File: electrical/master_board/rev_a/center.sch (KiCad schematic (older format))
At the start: 0 parts

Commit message: Updated some of the schematics and PCB's via hr2_models.py .
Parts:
- added CN50, CN54: HCSR04;F1X4, HR2:HCSR04_F1x4_MATE, symbol HR2:HCSR04;F1X4
- added CN51, CN52, CN53: HCSR04LP;F1X4, HR2:HCSR04_F1x4LP_MATE, symbol HR2:HCSR04LP;F1X4
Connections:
- no-connect marks 0 -> 20
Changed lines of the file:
@@
 Comment4 ""
 $EndDescr
+$Comp
+L HR2:HCSR04;F1X4 CN50
+U 1 1 5EE6C5CE
+P 2350 2550
+F 0 "CN50" H 2700 2700 50  0000 C CNN
+F 1 "HCSR04;F1X4" H 2700 2100 50  0000 C CNN
+F 2 "HR2:HCSR04_F1x4_MATE" H 2550 2600 60  0001 L CNN
+F 3 "https://cdn.sparkfun.com/datasheets/Sensors/Proximity/HCSR04.pdf" H 2550 2400 60  0001 L CNN
+F 4 "https://cdn.sparkfun.com/datasheets/Sensors/Proximity/HCSR04.pdf" H 2550 2500 60  0001 L CNN "manf#"
+F 5 "HC-SR04 Sonar (Normal Profile Receptacle)" H 2550 2300 60  0001 L CNN "Field5"
+	1    2350 2550
+	1    0    0    -1
+$EndComp
+$Comp
+L HR2:HCSR04;F1X4 CN54
+U 1 1 5EE6FA61
+P 5700 2550
+F 0 "CN54" H 6050 2700 50  0000 C CNN
+F 1 "HCSR04;F1X4" H 6050 2100 50  0000 C CNN
+F 2 "HR2:HCSR04_F1x4_MATE" H 5900 2600 60  0001 L CNN
+F 3 "https://cdn.sparkfun.com/datasheets/Sensors/Proximity/HCSR04.pdf" H 5900 2400 60  0001 L CNN
+F 4 "https://cdn.sparkfun.com/datasheets/Sensors/Proximity/HCSR04.pdf" H 5900 2500 60  0001 L CNN "manf#"
+F 5 "HC-SR04 Sonar (Normal Profile Receptacle)" H 5900 2300 60  0001 L CNN "Field5"
+	1    5700 2550
+	1    0    0    -1
+$EndComp
+NoConn ~ 3050 2550
+NoConn ~ 3050 2650
+NoConn ~ 3050 2750
+NoConn ~ 3050 2850
+NoConn ~ 3900 2550
+NoConn ~ 3900 2650
+NoConn ~ 3900 2750
+NoConn ~ 3900 2850
+NoConn ~ 4700 2550
+NoConn ~ 4700 2650
+NoConn ~ 4700 2750
+NoConn ~ 4700 2850
+NoConn ~ 5550 2550
+NoConn ~ 5550 2650
+NoConn ~ 5550 2750
+NoConn ~ 5550 2850
+NoConn ~ 6400 2550
+NoConn ~ 6400 2650
+NoConn ~ 6400 2750
+NoConn ~ 6400 2850
+$Comp
+L HR2:HCSR04LP;F1X4 CN51
+U 1 1 5EE6C7AA
+P 3200 2550
+F 0 "CN51" H 3550 2700 50  0000 C CNN
+F 1 "HCSR04LP;F1X4" H 3550 2100 50  0000 C CNN
+F 2 "HR2:HCSR04_F1x4LP_MATE" H 3400 2600 60  0001 L CNN
+F 3 "https://cdn.sparkfun.com/datasheets/Sensors/Proximity/HCSR04.pdf" H 3400 2400 60  0001 L CNN
+F 4 "https://cdn.sparkfun.com/datasheets/Sensors/Proximity/HCSR04.pdf" H 3400 2500 60  0001 L CNN "manf#"
+F 5 "HC-SR04 Sonar (Low Profile Receptacle)" H 3400 2300 60  0001 L CNN "Field5"
+	1    3200 2550
+	1    0    0    -1
+$EndComp
+$Comp
+L HR2:HCSR04LP;F1X4 CN52
+U 1 1 5EE6CD06
+P 4000 2550
+F 0 "CN52" H 4350 2700 50  0000 C CNN
+F 1 "HCSR04LP;F1X4" H 4350 2100 50  0000 C CNN
+F 2 "HR2:HCSR04_F1x4LP_MATE" H 4200 2600 60  0001 L CNN
+F 3 "https://cdn.sparkfun.com/datasheets/Sensors/Proximity/HCSR04.pdf" H 4200 2400 60  0001 L CNN
+F 4 "https://cdn.sparkfun.com/datasheets/Sensors/Proximity/HCSR04.pdf" H 4200 2500 60  0001 L CNN "manf#"
+F 5 "HC-SR04 Sonar (Low Profile Receptacle)" H 4200 2300 60  0001 L CNN "Field5"
+	1    4000 2550
+	1    0    0    -1
+$EndComp
+$Comp
+L HR2:HCSR04LP;F1X4 CN53
+U 1 1 5EE6D28F
+P 4850 2550
+F 0 "CN53" H 5200 2700 50  0000 C CNN
+F 1 "HCSR04LP;F1X4" H 5200 2100 50  0000 C CNN
+F 2 "HR2:HCSR04_F1x4LP_MATE" H 5050 2600 60  0001 L CNN
+F 3 "https://cdn.sparkfun.com/datasheets/Sensors/Proximity/HCSR04.pdf" H 5050 2400 60  0001 L CNN
+F 4 "https://cdn.sparkfun.com/datasheets/Sensors/Proximity/HCSR04.pdf" H 5050 2500 60  0001 L CNN "manf#"
+F 5 "HC-SR04 Sonar (Low Profile Receptacle)" H 5050 2300 60  0001 L CNN "Field5"
+	1    4850 2550
+	1    0    0    -1
+$EndComp
 $EndSCHEMATC

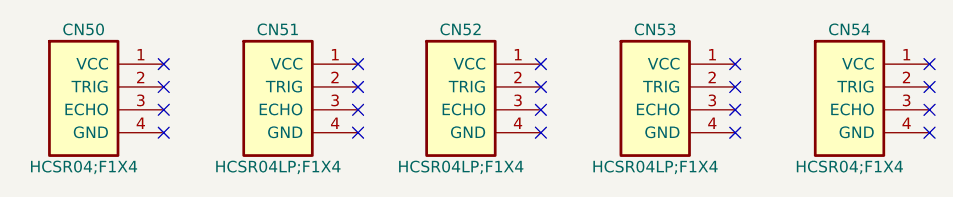
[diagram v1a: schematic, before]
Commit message: The PCBChunk'ification of Sonars is complete.
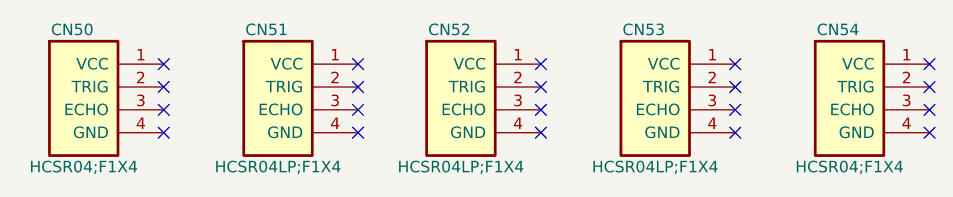
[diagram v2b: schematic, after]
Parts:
- CN50, CN54: footprint HR2:HCSR04_F1x4_MATE -> HR2:HCSR04_F1x4
- CN51, CN52, CN53: footprint HR2:HCSR04_F1x4LP_MATE -> HR2:HCSR04_F1x4LP
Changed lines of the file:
@@
 Comment4 ""
 $EndDescr
-$Comp
-L HR2:HCSR04;F1X4 CN50
-U 1 1 5EE6C5CE
-P 2350 2550
-F 0 "CN50" H 2700 2700 50  0000 C CNN
-F 1 "HCSR04;F1X4" H 2700 2100 50  0000 C CNN
-F 2 "HR2:HCSR04_F1x4_MATE" H 2550 2600 60  0001 L CNN
-F 3 "https://cdn.sparkfun.com/datasheets/Sensors/Proximity/HCSR04.pdf" H 2550 2400 60  0001 L CNN
-F 4 "https://cdn.sparkfun.com/datasheets/Sensors/Proximity/HCSR04.pdf" H 2550 2500 60  0001 L CNN "manf#"
-F 5 "HC-SR04 Sonar (Normal Profile Receptacle)" H 2550 2300 60  0001 L CNN "Field5"
-	1    2350 2550
-	1    0    0    -1
-$EndComp
-$Comp
-L HR2:HCSR04;F1X4 CN54
-U 1 1 5EE6FA61
-P 5700 2550
-F 0 "CN54" H 6050 2700 50  0000 C CNN
-F 1 "HCSR04;F1X4" H 6050 2100 50  0000 C CNN
-F 2 "HR2:HCSR04_F1x4_MATE" H 5900 2600 60  0001 L CNN
-F 3 "https://cdn.sparkfun.com/datasheets/Sensors/Proximity/HCSR04.pdf" H 5900 2400 60  0001 L CNN
-F 4 "https://cdn.sparkfun.com/datasheets/Sensors/Proximity/HCSR04.pdf" H 5900 2500 60  0001 L CNN "manf#"
-F 5 "HC-SR04 Sonar (Normal Profile Receptacle)" H 5900 2300 60  0001 L CNN "Field5"
-	1    5700 2550
-	1    0    0    -1
-$EndComp
 NoConn ~ 3050 2550
 NoConn ~ 3050 2650
@@
 $Comp
 L HR2:HCSR04LP;F1X4 CN51
-U 1 1 5EE6C7AA
+U 1 1 5F0BA517
 P 3200 2550
-F 0 "CN51" H 3550 2700 50  0000 C CNN
+F 0 "CN51" H 3500 2700 50  0000 C CNN
 F 1 "HCSR04LP;F1X4" H 3550 2100 50  0000 C CNN
-F 2 "HR2:HCSR04_F1x4LP_MATE" H 3400 2600 60  0001 L CNN
+F 2 "HR2:HCSR04_F1x4LP" H 3400 2600 60  0001 L CNN
 F 3 "https://cdn.sparkfun.com/datasheets/Sensors/Proximity/HCSR04.pdf" H 3400 2400 60  0001 L CNN
 F 4 "https://cdn.sparkfun.com/datasheets/Sensors/Proximity/HCSR04.pdf" H 3400 2500 60  0001 L CNN "manf#"
@@
 $Comp
 L HR2:HCSR04LP;F1X4 CN52
-U 1 1 5EE6CD06
+U 1 1 5F0BB7A6
 P 4000 2550
-F 0 "CN52" H 4350 2700 50  0000 C CNN
+F 0 "CN52" H 4300 2700 50  0000 C CNN
 F 1 "HCSR04LP;F1X4" H 4350 2100 50  0000 C CNN
-F 2 "HR2:HCSR04_F1x4LP_MATE" H 4200 2600 60  0001 L CNN
+F 2 "HR2:HCSR04_F1x4LP" H 4200 2600 60  0001 L CNN
 F 3 "https://cdn.sparkfun.com/datasheets/Sensors/Proximity/HCSR04.pdf" H 4200 2400 60  0001 L CNN
 F 4 "https://cdn.sparkfun.com/datasheets/Sensors/Proximity/HCSR04.pdf" H 4200 2500 60  0001 L CNN "manf#"
@@
 $Comp
 L HR2:HCSR04LP;F1X4 CN53
-U 1 1 5EE6D28F
+U 1 1 5F0BBC9F
 P 4850 2550
-F 0 "CN53" H 5200 2700 50  0000 C CNN
+F 0 "CN53" H 5150 2700 50  0000 C CNN
 F 1 "HCSR04LP;F1X4" H 5200 2100 50  0000 C CNN
-F 2 "HR2:HCSR04_F1x4LP_MATE" H 5050 2600 60  0001 L CNN
+F 2 "HR2:HCSR04_F1x4LP" H 5050 2600 60  0001 L CNN
 F 3 "https://cdn.sparkfun.com/datasheets/Sensors/Proximity/HCSR04.pdf" H 5050 2400 60  0001 L CNN
 F 4 "https://cdn.sparkfun.com/datasheets/Sensors/Proximity/HCSR04.pdf" H 5050 2500 60  0001 L CNN "manf#"
@@
 	1    0    0    -1
 $EndComp
+$Comp
+L HR2:HCSR04;F1X4 CN50
+U 1 1 5F0B87B8
+P 2350 2550
+F 0 "CN50" H 2650 2700 50  0000 C CNN
+F 1 "HCSR04;F1X4" H 2700 2100 50  0000 C CNN
+F 2 "HR2:HCSR04_F1x4" H 2550 2600 60  0001 L CNN
+F 3 "https://cdn.sparkfun.com/datasheets/Sensors/Proximity/HCSR04.pdf" H 2550 2400 60  0001 L CNN
+F 4 "https://cdn.sparkfun.com/datasheets/Sensors/Proximity/HCSR04.pdf" H 2550 2500 60  0001 L CNN "manf#"
+F 5 "HC-SR04 Sonar (Normal Profile Receptacle)" H 2550 2300 60  0001 L CNN "Field5"
+	1    2350 2550
+	1    0    0    -1
+$EndComp
+$Comp
+L HR2:HCSR04;F1X4 CN54
+U 1 1 5F0B915D
+P 5700 2550
+F 0 "CN54" H 6000 2700 50  0000 C CNN
+F 1 "HCSR04;F1X4" H 6050 2100 50  0000 C CNN
+F 2 "HR2:HCSR04_F1x4" H 5900 2600 60  0001 L CNN
+F 3 "https://cdn.sparkfun.com/datasheets/Sensors/Proximity/HCSR04.pdf" H 5900 2400 60  0001 L CNN
+F 4 "https://cdn.sparkfun.com/datasheets/Sensors/Proximity/HCSR04.pdf" H 5900 2500 60  0001 L CNN "manf#"
+F 5 "HC-SR04 Sonar (Normal Profile Receptacle)" H 5900 2300 60  0001 L CNN "Field5"
+	1    5700 2550
+	1    0    0    -1
+$EndComp

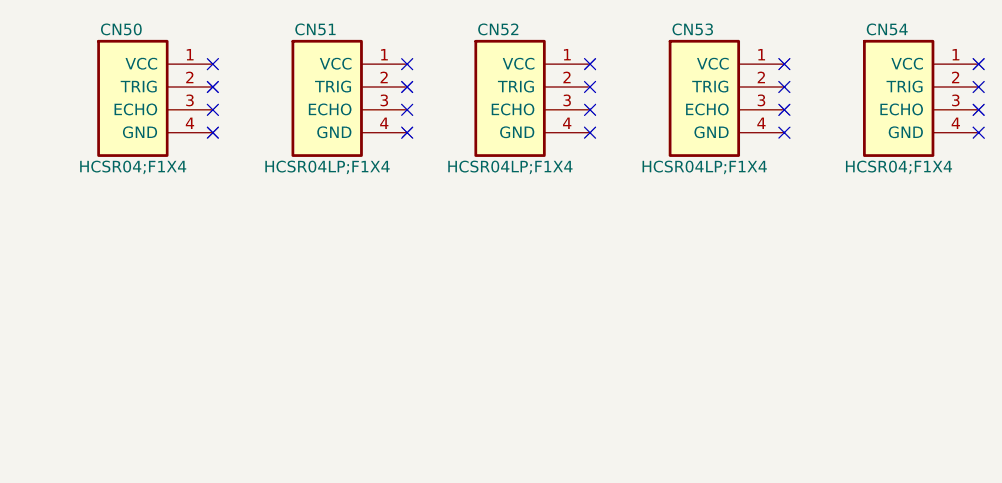
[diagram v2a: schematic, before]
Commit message: Got Encoder PCB's installed on the center PCB.
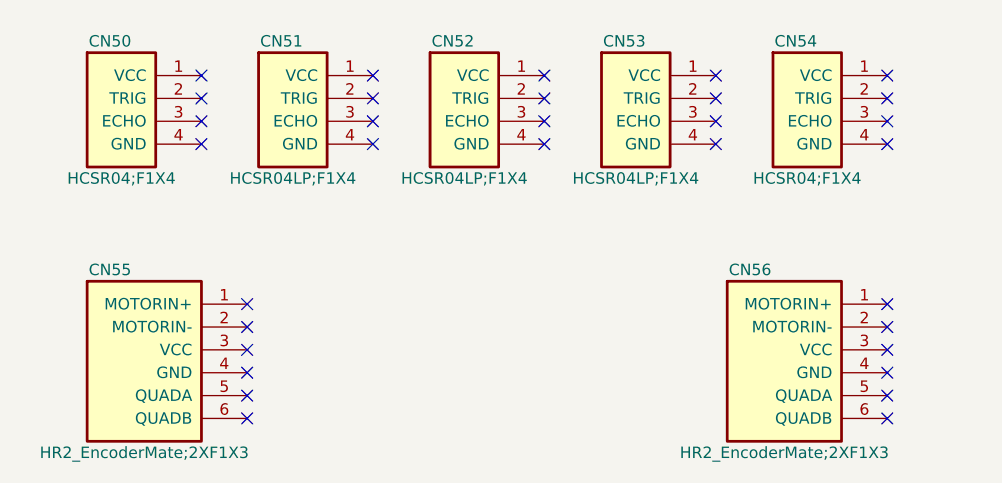
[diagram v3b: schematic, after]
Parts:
- added CN55, CN56: HR2_EncoderMate;2XF1X3, HR2:ENCODER_MATE, symbol HR2:HR2_EncoderMate;2XF1X3
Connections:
- no-connect marks 20 -> 32
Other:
- moved on the sheet: CN50, CN51, CN52, CN53, CN54
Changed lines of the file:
@@
 Comment4 ""
 $EndDescr
-NoConn ~ 3050 2550
-NoConn ~ 3050 2650
-NoConn ~ 3050 2750
-NoConn ~ 3050 2850
-NoConn ~ 3900 2550
-NoConn ~ 3900 2650
-NoConn ~ 3900 2750
-NoConn ~ 3900 2850
-NoConn ~ 4700 2550
-NoConn ~ 4700 2650
-NoConn ~ 4700 2750
-NoConn ~ 4700 2850
-NoConn ~ 5550 2550
-NoConn ~ 5550 2650
-NoConn ~ 5550 2750
-NoConn ~ 5550 2850
-NoConn ~ 6400 2550
-NoConn ~ 6400 2650
-NoConn ~ 6400 2750
-NoConn ~ 6400 2850
+NoConn ~ 3000 2600
+NoConn ~ 3000 2700
+NoConn ~ 3000 2800
+NoConn ~ 3000 2900
+NoConn ~ 3750 2600
+NoConn ~ 3750 2700
+NoConn ~ 3750 2800
+NoConn ~ 3750 2900
+NoConn ~ 4500 2600
+NoConn ~ 4500 2700
+NoConn ~ 4500 2800
+NoConn ~ 4500 2900
+NoConn ~ 5250 2600
+NoConn ~ 5250 2700
+NoConn ~ 5250 2800
+NoConn ~ 5250 2900
+NoConn ~ 6000 2600
+NoConn ~ 6000 2700
+NoConn ~ 6000 2800
+NoConn ~ 6000 2900
 $Comp
 L HR2:HCSR04LP;F1X4 CN51
 U 1 1 5F0BA517
-P 3200 2550
-F 0 "CN51" H 3500 2700 50  0000 C CNN
-F 1 "HCSR04LP;F1X4" H 3550 2100 50  0000 C CNN
-F 2 "HR2:HCSR04_F1x4LP" H 3400 2600 60  0001 L CNN
-F 3 "https://cdn.sparkfun.com/datasheets/Sensors/Proximity/HCSR04.pdf" H 3400 2400 60  0001 L CNN
-F 4 "https://cdn.sparkfun.com/datasheets/Sensors/Proximity/HCSR04.pdf" H 3400 2500 60  0001 L CNN "manf#"
-F 5 "HC-SR04 Sonar (Low Profile Receptacle)" H 3400 2300 60  0001 L CNN "Field5"
-	1    3200 2550
+P 3050 2600
+F 0 "CN51" H 3350 2750 50  0000 C CNN
+F 1 "HCSR04LP;F1X4" H 3400 2150 50  0000 C CNN
+F 2 "HR2:HCSR04_F1x4LP" H 3250 2650 60  0001 L CNN
+F 3 "https://cdn.sparkfun.com/datasheets/Sensors/Proximity/HCSR04.pdf" H 3250 2450 60  0001 L CNN
+F 4 "https://cdn.sparkfun.com/datasheets/Sensors/Proximity/HCSR04.pdf" H 3250 2550 60  0001 L CNN "manf#"
+F 5 "HC-SR04 Sonar (Low Profile Receptacle)" H 3250 2350 60  0001 L CNN "Field5"
+	1    3050 2600
 	1    0    0    -1
 $EndComp
@@
 L HR2:HCSR04LP;F1X4 CN52
 U 1 1 5F0BB7A6
-P 4000 2550
-F 0 "CN52" H 4300 2700 50  0000 C CNN
-F 1 "HCSR04LP;F1X4" H 4350 2100 50  0000 C CNN
-F 2 "HR2:HCSR04_F1x4LP" H 4200 2600 60  0001 L CNN
-F 3 "https://cdn.sparkfun.com/datasheets/Sensors/Proximity/HCSR04.pdf" H 4200 2400 60  0001 L CNN
-F 4 "https://cdn.sparkfun.com/datasheets/Sensors/Proximity/HCSR04.pdf" H 4200 2500 60  0001 L CNN "manf#"
-F 5 "HC-SR04 Sonar (Low Profile Receptacle)" H 4200 2300 60  0001 L CNN "Field5"
-	1    4000 2550
+P 3800 2600
+F 0 "CN52" H 4100 2750 50  0000 C CNN
+F 1 "HCSR04LP;F1X4" H 4150 2150 50  0000 C CNN
+F 2 "HR2:HCSR04_F1x4LP" H 4000 2650 60  0001 L CNN
+F 3 "https://cdn.sparkfun.com/datasheets/Sensors/Proximity/HCSR04.pdf" H 4000 2450 60  0001 L CNN
+F 4 "https://cdn.sparkfun.com/datasheets/Sensors/Proximity/HCSR04.pdf" H 4000 2550 60  0001 L CNN "manf#"
+F 5 "HC-SR04 Sonar (Low Profile Receptacle)" H 4000 2350 60  0001 L CNN "Field5"
+	1    3800 2600
 	1    0    0    -1
 $EndComp
@@
 L HR2:HCSR04LP;F1X4 CN53
 U 1 1 5F0BBC9F
-P 4850 2550
-F 0 "CN53" H 5150 2700 50  0000 C CNN
-F 1 "HCSR04LP;F1X4" H 5200 2100 50  0000 C CNN
-F 2 "HR2:HCSR04_F1x4LP" H 5050 2600 60  0001 L CNN
-F 3 "https://cdn.sparkfun.com/datasheets/Sensors/Proximity/HCSR04.pdf" H 5050 2400 60  0001 L CNN
-F 4 "https://cdn.sparkfun.com/datasheets/Sensors/Proximity/HCSR04.pdf" H 5050 2500 60  0001 L CNN "manf#"
-F 5 "HC-SR04 Sonar (Low Profile Receptacle)" H 5050 2300 60  0001 L CNN "Field5"
-	1    4850 2550
+P 4550 2600
+F 0 "CN53" H 4850 2750 50  0000 C CNN
+F 1 "HCSR04LP;F1X4" H 4900 2150 50  0000 C CNN
+F 2 "HR2:HCSR04_F1x4LP" H 4750 2650 60  0001 L CNN
+F 3 "https://cdn.sparkfun.com/datasheets/Sensors/Proximity/HCSR04.pdf" H 4750 2450 60  0001 L CNN
+F 4 "https://cdn.sparkfun.com/datasheets/Sensors/Proximity/HCSR04.pdf" H 4750 2550 60  0001 L CNN "manf#"
+F 5 "HC-SR04 Sonar (Low Profile Receptacle)" H 4750 2350 60  0001 L CNN "Field5"
+	1    4550 2600
 	1    0    0    -1
 $EndComp
@@
 L HR2:HCSR04;F1X4 CN50
 U 1 1 5F0B87B8
-P 2350 2550
-F 0 "CN50" H 2650 2700 50  0000 C CNN
-F 1 "HCSR04;F1X4" H 2700 2100 50  0000 C CNN
-F 2 "HR2:HCSR04_F1x4" H 2550 2600 60  0001 L CNN
-F 3 "https://cdn.sparkfun.com/datasheets/Sensors/Proximity/HCSR04.pdf" H 2550 2400 60  0001 L CNN
-F 4 "https://cdn.sparkfun.com/datasheets/Sensors/Proximity/HCSR04.pdf" H 2550 2500 60  0001 L CNN "manf#"
-F 5 "HC-SR04 Sonar (Normal Profile Receptacle)" H 2550 2300 60  0001 L CNN "Field5"
-	1    2350 2550
+P 2300 2600
+F 0 "CN50" H 2600 2750 50  0000 C CNN
+F 1 "HCSR04;F1X4" H 2650 2150 50  0000 C CNN
+F 2 "HR2:HCSR04_F1x4" H 2500 2650 60  0001 L CNN
+F 3 "https://cdn.sparkfun.com/datasheets/Sensors/Proximity/HCSR04.pdf" H 2500 2450 60  0001 L CNN
+F 4 "https://cdn.sparkfun.com/datasheets/Sensors/Proximity/HCSR04.pdf" H 2500 2550 60  0001 L CNN "manf#"
+F 5 "HC-SR04 Sonar (Normal Profile Receptacle)" H 2500 2350 60  0001 L CNN "Field5"
+	1    2300 2600
 	1    0    0    -1
 $EndComp
@@
 L HR2:HCSR04;F1X4 CN54
 U 1 1 5F0B915D
-P 5700 2550
-F 0 "CN54" H 6000 2700 50  0000 C CNN
-F 1 "HCSR04;F1X4" H 6050 2100 50  0000 C CNN
-F 2 "HR2:HCSR04_F1x4" H 5900 2600 60  0001 L CNN
-F 3 "https://cdn.sparkfun.com/datasheets/Sensors/Proximity/HCSR04.pdf" H 5900 2400 60  0001 L CNN
-F 4 "https://cdn.sparkfun.com/datasheets/Sensors/Proximity/HCSR04.pdf" H 5900 2500 60  0001 L CNN "manf#"
-F 5 "HC-SR04 Sonar (Normal Profile Receptacle)" H 5900 2300 60  0001 L CNN "Field5"
-	1    5700 2550
+P 5300 2600
+F 0 "CN54" H 5600 2750 50  0000 C CNN
+F 1 "HCSR04;F1X4" H 5650 2150 50  0000 C CNN
+F 2 "HR2:HCSR04_F1x4" H 5500 2650 60  0001 L CNN
+F 3 "https://cdn.sparkfun.com/datasheets/Sensors/Proximity/HCSR04.pdf" H 5500 2450 60  0001 L CNN
+F 4 "https://cdn.sparkfun.com/datasheets/Sensors/Proximity/HCSR04.pdf" H 5500 2550 60  0001 L CNN "manf#"
+F 5 "HC-SR04 Sonar (Normal Profile Receptacle)" H 5500 2350 60  0001 L CNN "Field5"
+	1    5300 2600
 	1    0    0    -1
 $EndComp
+NoConn ~ 3200 3600
+NoConn ~ 3200 3700
+NoConn ~ 3200 3800
+NoConn ~ 3200 3900
+NoConn ~ 3200 4000
+NoConn ~ 3200 4100
+$Comp
+L HR2:HR2_EncoderMate;2XF1X3 CN55
+U 1 1 5F0BB3ED
+P 2300 3600
+F 0 "CN55" H 2600 3750 50  0000 C CNN
+F 1 "HR2_EncoderMate;2XF1X3" H 2750 2950 50  0000 C CNN
+F 2 "HR2:ENCODER_MATE" H 2500 3650 60  0001 L CNN
+F 3 "HR2 Encoder Mating Connector" H 2500 3450 60  0001 L CNN
+F 4 "HR2 Encoder Mating Connector" H 2500 3350 60  0001 L CNN "Field5"
+	1    2300 3600
+	1    0    0    -1
+$EndComp
+NoConn ~ 6000 4100
+NoConn ~ 6000 4000
+NoConn ~ 6000 3900
+NoConn ~ 6000 3800
+NoConn ~ 6000 3700
+NoConn ~ 6000 3600
+$Comp
+L HR2:HR2_EncoderMate;2XF1X3 CN56
+U 1 1 5F0BC2D6
+P 5100 3600
+F 0 "CN56" H 5400 3750 50  0000 C CNN
+F 1 "HR2_EncoderMate;2XF1X3" H 5550 2950 50  0000 C CNN
+F 2 "HR2:ENCODER_MATE" H 5300 3650 60  0001 L CNN
+F 3 "HR2 Encoder Mating Connector" H 5300 3450 60  0001 L CNN
+F 4 "HR2 Encoder Mating Connector" H 5300 3350 60  0001 L CNN "Field5"
+	1    5100 3600
+	1    0    0    -1
+$EndComp

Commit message: Added Raspbery Pi F2x20 Connector to schematic library.
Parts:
- added CN57: RASPI;F2X20;HR2_RASPI_F2X20, symbol HR2:RASPI;F2X20;HR2_RASPI_F2X20
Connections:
- no-connect marks 32 -> 72
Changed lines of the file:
@@
-	1    0    0    -1
-$EndComp
-$Comp
-L HR2:HCSR04;F1X4 CN50
-U 1 1 5F0B87B8
-P 2300 2600
-F 0 "CN50" H 2600 2750 50  0000 C CNN
-F 1 "HCSR04;F1X4" H 2650 2150 50  0000 C CNN
-F 2 "HR2:HCSR04_F1x4" H 2500 2650 60  0001 L CNN
-F 3 "https://cdn.sparkfun.com/datasheets/Sensors/Proximity/HCSR04.pdf" H 2500 2450 60  0001 L CNN
-F 4 "https://cdn.sparkfun.com/datasheets/Sensors/Proximity/HCSR04.pdf" H 2500 2550 60  0001 L CNN "manf#"
-F 5 "HC-SR04 Sonar (Normal Profile Receptacle)" H 2500 2350 60  0001 L CNN "Field5"
-	1    2300 2600
-	1    0    0    -1
-$EndComp
-$Comp
-L HR2:HCSR04;F1X4 CN54
-U 1 1 5F0B915D
-P 5300 2600
-F 0 "CN54" H 5600 2750 50  0000 C CNN
-F 1 "HCSR04;F1X4" H 5650 2150 50  0000 C CNN
-F 2 "HR2:HCSR04_F1x4" H 5500 2650 60  0001 L CNN
-F 3 "https://cdn.sparkfun.com/datasheets/Sensors/Proximity/HCSR04.pdf" H 5500 2450 60  0001 L CNN
-F 4 "https://cdn.sparkfun.com/datasheets/Sensors/Proximity/HCSR04.pdf" H 5500 2550 60  0001 L CNN "manf#"
-F 5 "HC-SR04 Sonar (Normal Profile Receptacle)" H 5500 2350 60  0001 L CNN "Field5"
-	1    5300 2600
 	1    0    0    -1
 $EndComp
@@
 	1    0    0    -1
 $EndComp
+$Comp
+L HR2:HCSR04;F1X4 CN50
+U 1 1 5F0D2697
+P 2300 2600
+F 0 "CN50" H 2650 2750 50  0000 C CNN
+F 1 "HCSR04;F1X4" H 2650 2150 50  0000 C CNN
+F 2 "HR2:HCSR04_F1x4" H 2500 2650 60  0001 L CNN
+F 3 "HC-SR04" H 2500 2450 60  0001 L CNN
+F 4 "https://cdn.sparkfun.com/datasheets/Sensors/Proximity/HCSR04.pdf" H 2500 2550 60  0001 L CNN "manf#"
+F 5 "HC-SR04 Sonar (Normal Profile Receptacle)" H 2500 2350 60  0001 L CNN "Field5"
+	1    2300 2600
+	1    0    0    -1
+$EndComp
+$Comp
+L HR2:HCSR04;F1X4 CN54
+U 1 1 5F0D2FF0
+P 5300 2600
+F 0 "CN54" H 5650 2750 50  0000 C CNN
+F 1 "HCSR04;F1X4" H 5650 2150 50  0000 C CNN
+F 2 "HR2:HCSR04_F1x4" H 5500 2650 60  0001 L CNN
+F 3 "HC-SR04" H 5500 2450 60  0001 L CNN
+F 4 "https://cdn.sparkfun.com/datasheets/Sensors/Proximity/HCSR04.pdf" H 5500 2550 60  0001 L CNN "manf#"
+F 5 "HC-SR04 Sonar (Normal Profile Receptacle)" H 5500 2350 60  0001 L CNN "Field5"
+	1    5300 2600
+	1    0    0    -1
+$EndComp
+$Comp
+L HR2:RASPI;F2X20;HR2_RASPI_F2X20 CN57
+U 1 1 5F0D2725
+P 7600 1000
+F 0 "CN57" H 8050 1150 60  0000 C CNN
+F 1 "RASPI;F2X20;HR2_RASPI_F2X20" H 8050 -3050 60  0000 C CNN
+F 2 "" H 7800 1050 60  0001 L CNN
+F 3 "HR2 Raspberry Pi F2x20 Connector" H 7800 850 60  0001 L CNN
+	1    7600 1000
+	1    0    0    -1
+$EndComp
+NoConn ~ 8500 1000
+NoConn ~ 8500 1100
+NoConn ~ 8500 1200
+NoConn ~ 8500 1300
+NoConn ~ 8500 1400
+NoConn ~ 8500 1500
+NoConn ~ 8500 1600
+NoConn ~ 8500 1700
+NoConn ~ 8500 1800
+NoConn ~ 8500 1900
+NoConn ~ 8500 2000
+NoConn ~ 8500 2100
+NoConn ~ 8500 2200
+NoConn ~ 8500 2300
+NoConn ~ 8500 2400
+NoConn ~ 8500 2500
+NoConn ~ 8500 2600
+NoConn ~ 8500 2700
+NoConn ~ 8500 2800
+NoConn ~ 8500 2900
+NoConn ~ 8500 3000
+NoConn ~ 8500 3100
+NoConn ~ 8500 3200
+NoConn ~ 8500 3300
+NoConn ~ 8500 3400
+NoConn ~ 8500 3500
+NoConn ~ 8500 3600
+NoConn ~ 8500 3700
+NoConn ~ 8500 3800
+NoConn ~ 8500 3900
+NoConn ~ 8500 4000
+NoConn ~ 8500 4100
+NoConn ~ 8500 4900
+NoConn ~ 8500 4800
+NoConn ~ 8500 4700
+NoConn ~ 8500 4600
+NoConn ~ 8500 4500
+NoConn ~ 8500 4400
+NoConn ~ 8500 4300
+NoConn ~ 8500 4200
 $EndSCHEMATC

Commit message: Did initial placement of RasPi4B+ (at origin).
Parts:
- removed CN57: RASPI;F2X20;HR2_RASPI_F2X20, symbol HR2:RASPI;F2X20;HR2_RASPI_F2X20
- added CN57: RASPI;F2X20, HR2:RASPI_F2X20, symbol HR2:RASPI;F2X20
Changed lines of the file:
@@
-	1    0    0    -1
-$EndComp
-$Comp
-L HR2:RASPI;F2X20;HR2_RASPI_F2X20 CN57
-U 1 1 5F0D2725
-P 7600 1000
-F 0 "CN57" H 8050 1150 60  0000 C CNN
-F 1 "RASPI;F2X20;HR2_RASPI_F2X20" H 8050 -3050 60  0000 C CNN
-F 2 "" H 7800 1050 60  0001 L CNN
-F 3 "HR2 Raspberry Pi F2x20 Connector" H 7800 850 60  0001 L CNN
-	1    7600 1000
 	1    0    0    -1
 $EndComp
@@
 NoConn ~ 8500 4300
 NoConn ~ 8500 4200
+$Comp
+L HR2:RASPI;F2X20 CN57
+U 1 1 5F1114B0
+P 7600 1000
+F 0 "CN57" H 8050 1150 50  0000 C CNN
+F 1 "RASPI;F2X20" H 8050 -3050 50  0000 C CNN
+F 2 "HR2:RASPI_F2X20" H 7800 1050 60  0001 L CNN
+F 3 "Raspberry Pi F2x20 Connector (Row Swappped)" H 7800 850 60  0001 L CNN
+	1    7600 1000
+	1    0    0    -1
+$EndComp
 $EndSCHEMATC
